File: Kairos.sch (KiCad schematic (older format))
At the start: 40 parts, among them J1 USB_mini_micro_B, Q1 NSS40301MZ4T1G, SW1 SW_RST1, U1 ATMEGA32U2-AU, Y1 Crystal

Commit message: Rotated ISO enter stabs
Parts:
- C1, C2, C3, C5, C6: footprint (none) -> Capacitors_SMD:C_0603
- C4: footprint (none) -> Capacitors_SMD:C_0805
- F1: footprint (none) -> Fuse_Holders_and_Fuses:Fuse_SMD1206_Reflow
- R1, R2, R3, R4: footprint (none) -> Resistors_SMD:R_0603
- U1: footprint (none) -> Housings_DFN_QFN:QFN-32-1EP_5x5mm_Pitch0.5mm
- Y1: footprint (none) -> Crystals:Crystal_SMD_5032-2pin_5.0x3.2mm
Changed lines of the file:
@@
 F 0 "U1" H 2200 4400 50  0000 C CNN
 F 1 "ATMEGA32U2-AU" H 3800 1700 50  0000 C CNN
-F 2 "" H 2900 3100 50  0001 C CNN
+F 2 "Housings_DFN_QFN:QFN-32-1EP_5x5mm_Pitch0.5mm" H 2900 3100 50  0001 C CNN
 F 3 "http://www.atmel.com/Images/doc7799.pdf" H 3150 1600 50  0001 C CNN
 	1    3050 3050
@@
 F 0 "R1" V 4480 3550 50  0000 C CNN
 F 1 "10k" V 4400 3550 50  0000 C CNN
-F 2 "" V 4330 3550 50  0001 C CNN
+F 2 "Resistors_SMD:R_0603" V 4330 3550 50  0001 C CNN
 F 3 "" H 4400 3550 50  0001 C CNN
 	1    4400 3550
@@
 F 0 "R2" V 1480 3450 50  0000 C CNN
 F 1 "22" V 1400 3450 50  0000 C CNN
-F 2 "" V 1330 3450 50  0001 C CNN
+F 2 "Resistors_SMD:R_0603" V 1330 3450 50  0001 C CNN
 F 3 "" H 1400 3450 50  0001 C CNN
 	1    1400 3450
@@
 F 0 "R3" V 1180 3550 50  0000 C CNN
 F 1 "22" V 1100 3550 50  0000 C CNN
-F 2 "" V 1030 3550 50  0001 C CNN
+F 2 "Resistors_SMD:R_0603" V 1030 3550 50  0001 C CNN
 F 3 "" H 1100 3550 50  0001 C CNN
 	1    1100 3550
@@
 F 0 "C1" V 1300 3300 50  0000 L CNN
 F 1 "1uF" V 1300 3050 50  0000 L CNN
-F 2 "" H 1388 3100 50  0001 C CNN
+F 2 "Capacitors_SMD:C_0603" H 1388 3100 50  0001 C CNN
 F 3 "" H 1350 3250 50  0001 C CNN
 	1    1350 3250
@@
 F 0 "R4" V 1480 2350 50  0000 C CNN
 F 1 "10k" V 1400 2350 50  0000 C CNN
-F 2 "" V 1330 2350 50  0001 C CNN
+F 2 "Resistors_SMD:R_0603" V 1330 2350 50  0001 C CNN
 F 3 "" H 1400 2350 50  0001 C CNN
 	1    1400 2350
@@
 F 0 "C2" H 725 1500 50  0000 L CNN
 F 1 "100nF" H 725 1300 50  0000 L CNN
-F 2 "" H 738 1250 50  0001 C CNN
+F 2 "Capacitors_SMD:C_0603" H 738 1250 50  0001 C CNN
 F 3 "" H 700 1400 50  0001 C CNN
 	1    700  1400
@@
 F 0 "C3" H 1025 1500 50  0000 L CNN
 F 1 "100nF" H 1025 1300 50  0000 L CNN
-F 2 "" H 1038 1250 50  0001 C CNN
+F 2 "Capacitors_SMD:C_0603" H 1038 1250 50  0001 C CNN
 F 3 "" H 1000 1400 50  0001 C CNN
 	1    1000 1400
@@
 F 0 "C4" H 1325 1500 50  0000 L CNN
 F 1 "4.7uF" H 1325 1300 50  0000 L CNN
-F 2 "" H 1338 1250 50  0001 C CNN
+F 2 "Capacitors_SMD:C_0805" H 1338 1250 50  0001 C CNN
 F 3 "" H 1300 1400 50  0001 C CNN
 	1    1300 1400
@@
 F 0 "Y1" H 1550 2850 50  0000 C CNN
 F 1 "Crystal" H 1550 2550 50  0000 C CNN
-F 2 "" H 1550 2700 50  0001 C CNN
+F 2 "Crystals:Crystal_SMD_5032-2pin_5.0x3.2mm" H 1550 2700 50  0001 C CNN
 F 3 "" H 1550 2700 50  0001 C CNN
 	1    1550 2700
@@
 F 0 "C6" H 1125 2650 50  0000 L CNN
 F 1 "22pF" H 1125 2450 50  0000 L CNN
-F 2 "" H 1138 2400 50  0001 C CNN
+F 2 "Capacitors_SMD:C_0603" H 1138 2400 50  0001 C CNN
 F 3 "" H 1100 2550 50  0001 C CNN
 	1    1100 2550
@@
 F 0 "C5" H 1125 2950 50  0000 L CNN
 F 1 "22pF" H 1125 2750 50  0000 L CNN
-F 2 "" H 1138 2700 50  0001 C CNN
+F 2 "Capacitors_SMD:C_0603" H 1138 2700 50  0001 C CNN
 F 3 "" H 1100 2850 50  0001 C CNN
 	1    1100 2850
@@
 F 0 "F1" V 1350 4300 50  0000 C CNN
 F 1 "Polyfuse" V 1550 4300 50  0000 C CNN
-F 2 "" H 1500 4100 50  0001 L CNN
+F 2 "Fuse_Holders_and_Fuses:Fuse_SMD1206_Reflow" H 1500 4100 50  0001 L CNN
 F 3 "" H 1450 4300 50  0001 C CNN
 	1    1450 4300

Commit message: Update associations for transistor and TQFP-ify the controller
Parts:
- Q1: footprint (none) -> TO_SOT_Packages_SMD:SOT-223-3Lead_TabPin2
- U1: footprint Housings_DFN_QFN:QFN-32-1EP_5x5mm_Pitch0.5mm -> Housings_QFP:TQFP-32_7x7mm_Pitch0.8mm
- Y1: footprint Crystals:Crystal_SMD_5032-2pin_5.0x3.2mm -> Crystals:Crystal_SMD_3225-4pin_3.2x2.5mm
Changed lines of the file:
@@
 F 0 "U1" H 2200 4400 50  0000 C CNN
 F 1 "ATMEGA32U2-AU" H 3800 1700 50  0000 C CNN
-F 2 "Housings_DFN_QFN:QFN-32-1EP_5x5mm_Pitch0.5mm" H 2900 3100 50  0001 C CNN
+F 2 "Housings_QFP:TQFP-32_7x7mm_Pitch0.8mm" H 2900 3100 50  0001 C CNN
 F 3 "http://www.atmel.com/Images/doc7799.pdf" H 3150 1600 50  0001 C CNN
 	1    3050 3050
@@
 F 0 "Y1" H 1550 2850 50  0000 C CNN
 F 1 "Crystal" H 1550 2550 50  0000 C CNN
-F 2 "Crystals:Crystal_SMD_5032-2pin_5.0x3.2mm" H 1550 2700 50  0001 C CNN
+F 2 "Crystals:Crystal_SMD_3225-4pin_3.2x2.5mm" H 1550 2700 50  0001 C CNN
 F 3 "" H 1550 2700 50  0001 C CNN
 	1    1550 2700
@@
 F 0 "Q1" H 4150 1275 50  0000 L CNN
 F 1 "NSS40301MZ4T1G" H 4150 1200 50  0000 L CNN
-F 2 "" H 4150 1125 50  0001 L CIN
+F 2 "TO_SOT_Packages_SMD:SOT-223-3Lead_TabPin2" H 4150 1125 50  0001 L CIN
 F 3 "" H 3950 1200 50  0001 L CNN
 	1    3950 1200

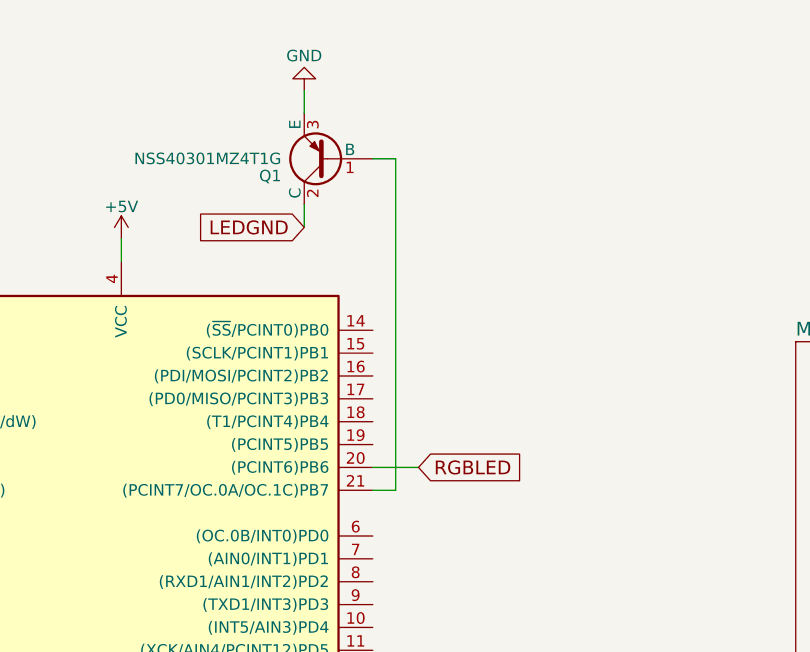
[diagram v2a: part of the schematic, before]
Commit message: Add missing 1.5k resistor on LED PWM
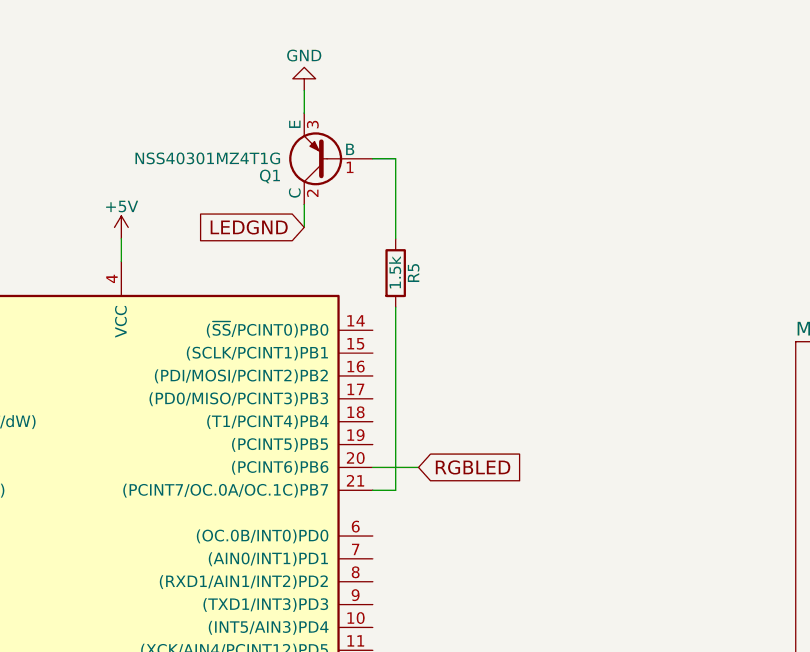
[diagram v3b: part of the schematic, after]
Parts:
- added R5: 1.5k, Resistors_SMD:R_0603, symbol R
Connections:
- net at U1.21 ((PCINT7/OC.0A/OC.1C)PB7): now also R5.2; no longer Q1.1 (B)
- new net: Q1.1 (B), R5.1
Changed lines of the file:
@@
 	4150 2650 4250 2650
-Wire Wire Line
-	4250 2650 4250 1200
 Wire Wire Line
 	4250 1200 4150 1200
@@
 NoConn ~ 1150 4600
 NoConn ~ 1150 4800
+$Comp
+L R R5
+U 1 1 59512333
+P 4250 1700
+F 0 "R5" V 4330 1700 50  0000 C CNN
+F 1 "1.5k" V 4250 1700 50  0000 C CNN
+F 2 "Resistors_SMD:R_0603" V 4180 1700 50  0001 C CNN
+F 3 "" H 4250 1700 50  0001 C CNN
+	1    4250 1700
+	1    0    0    -1
+$EndComp
+Wire Wire Line
+	4250 1200 4250 1550
+Wire Wire Line
+	4250 2650 4250 1850
 $EndSCHEMATC

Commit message: Fix the crystal
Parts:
- removed Y1: Crystal, Crystals:Crystal_SMD_3225-4pin_3.2x2.5mm, symbol Crystal
- added Y1: Crystal_GND24, Crystals:Crystal_SMD_3225-4pin_3.2x2.5mm, symbol Crystal_GND24
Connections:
- net GND: now also Y1.2, Y1.4
- net at C6.1, U1.1 (XTAL1): now also Y1.1
- net at C5.1, U1.2 (PC0(XTAL2)): now also Y1.3

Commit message: Add lib, update schematic
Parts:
- removed J1: USB_mini_micro_B, symbol USB_mini_micro_B
- added USB1: Molex-0548190589, symbol Molex-0548190589
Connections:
- net DM: now also USB1.4 (D-)
- net DP: now also USB1.3 (D+)
- net GND: now also USB1.1 (GND)
- net VCC: now also USB1.5 (VBUS)
- no-connect marks 3 -> 2
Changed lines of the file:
@@
 LIBS:ws2812b
 LIBS:keyboard_parts
+LIBS:Molex-0548190589
 LIBS:Kairos-cache
 EELAYER 25 0
@@
 $EndComp
 NoConn ~ 10000 6150
-$Comp
-L USB_mini_micro_B J1
-U 1 1 5947BA25
-P 1000 4450
-F 0 "J1" H 600 4400 60  0000 C CNN
-F 1 "USB_mini_micro_B" H 850 4700 60  0001 C CNN
-F 2 "" H 950 4450 60  0001 C CNN
-F 3 "" H 950 4450 60  0000 C CNN
-	1    1000 4450
-	1    0    0    -1
-$EndComp
 NoConn ~ 1150 4600
-NoConn ~ 1150 4800
 $Comp
 L R R5
@@
 	1350 2950 1350 2700
 Connection ~ 1950 2950
+$Comp
+L Molex-0548190589 USB1
+U 1 1 59859F20
+P 850 4500
+F 0 "USB1" H 850 4700 60  0000 C CNN
+F 1 "Molex-0548190589" H 850 4800 60  0000 C CNN
+F 2 "" H 850 4500 60  0001 C CNN
+F 3 "" H 850 4500 60  0001 C CNN
+	1    850  4500
+	0    -1   -1   0
+$EndComp
 $EndSCHEMATC

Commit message: Add that USB port
Not placed correctly yet
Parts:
- USB1: footprint (none) -> Molex-0548190589:Molex-0548190589
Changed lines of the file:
@@
 F 0 "USB1" H 850 4700 60  0000 C CNN
 F 1 "Molex-0548190589" H 850 4800 60  0000 C CNN
-F 2 "" H 850 4500 60  0001 C CNN
+F 2 "Molex-0548190589:Molex-0548190589" H 850 4500 60  0001 C CNN
 F 3 "" H 850 4500 60  0001 C CNN
 	1    850  4500

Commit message: Add reset button
Unlocked outline footprint to measure dimensions
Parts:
- SW1: footprint (none) -> Molex-0548190589:PushButton_6x6mm_TH
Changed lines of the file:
@@
 F 0 "SW1" H 1750 2260 50  0000 C CNN
 F 1 "SW_RST1" H 1600 2070 50  0000 C CNN
-F 2 "" H 1600 2150 60  0001 C CNN
+F 2 "Molex-0548190589:PushButton_6x6mm_TH" H 1600 2150 60  0001 C CNN
 F 3 "" H 1600 2150 60  0000 C CNN
 	1    1600 2150

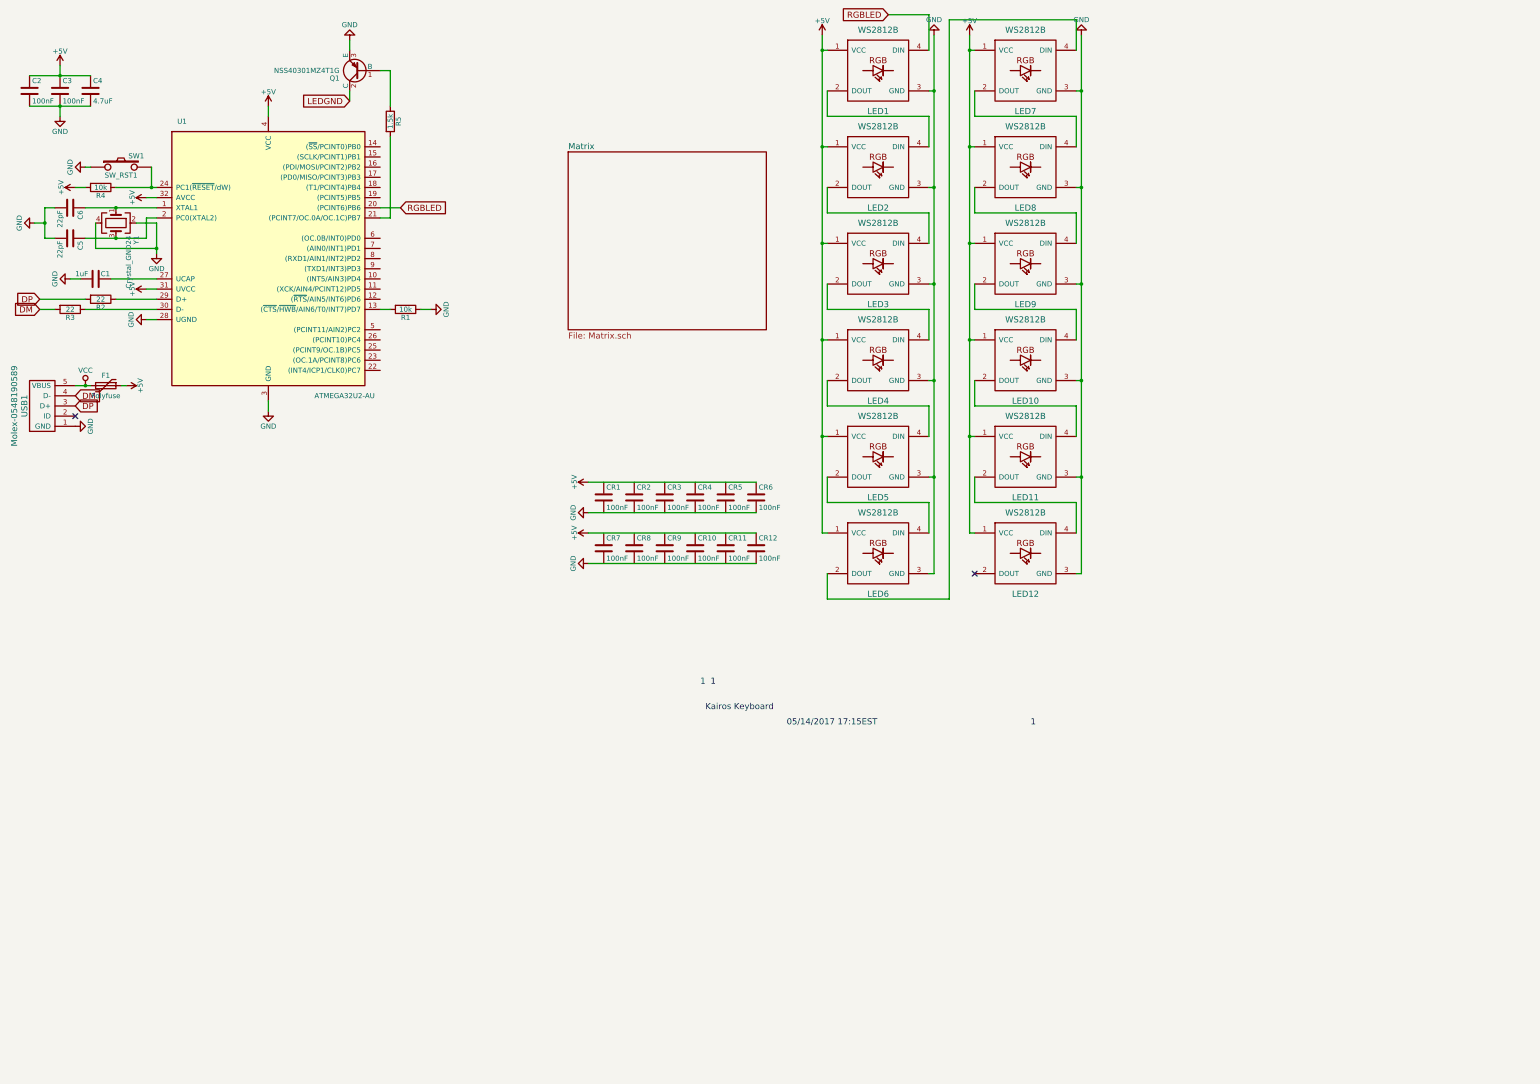
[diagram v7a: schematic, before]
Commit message: Add 2 more RGBs and their decoupling caps
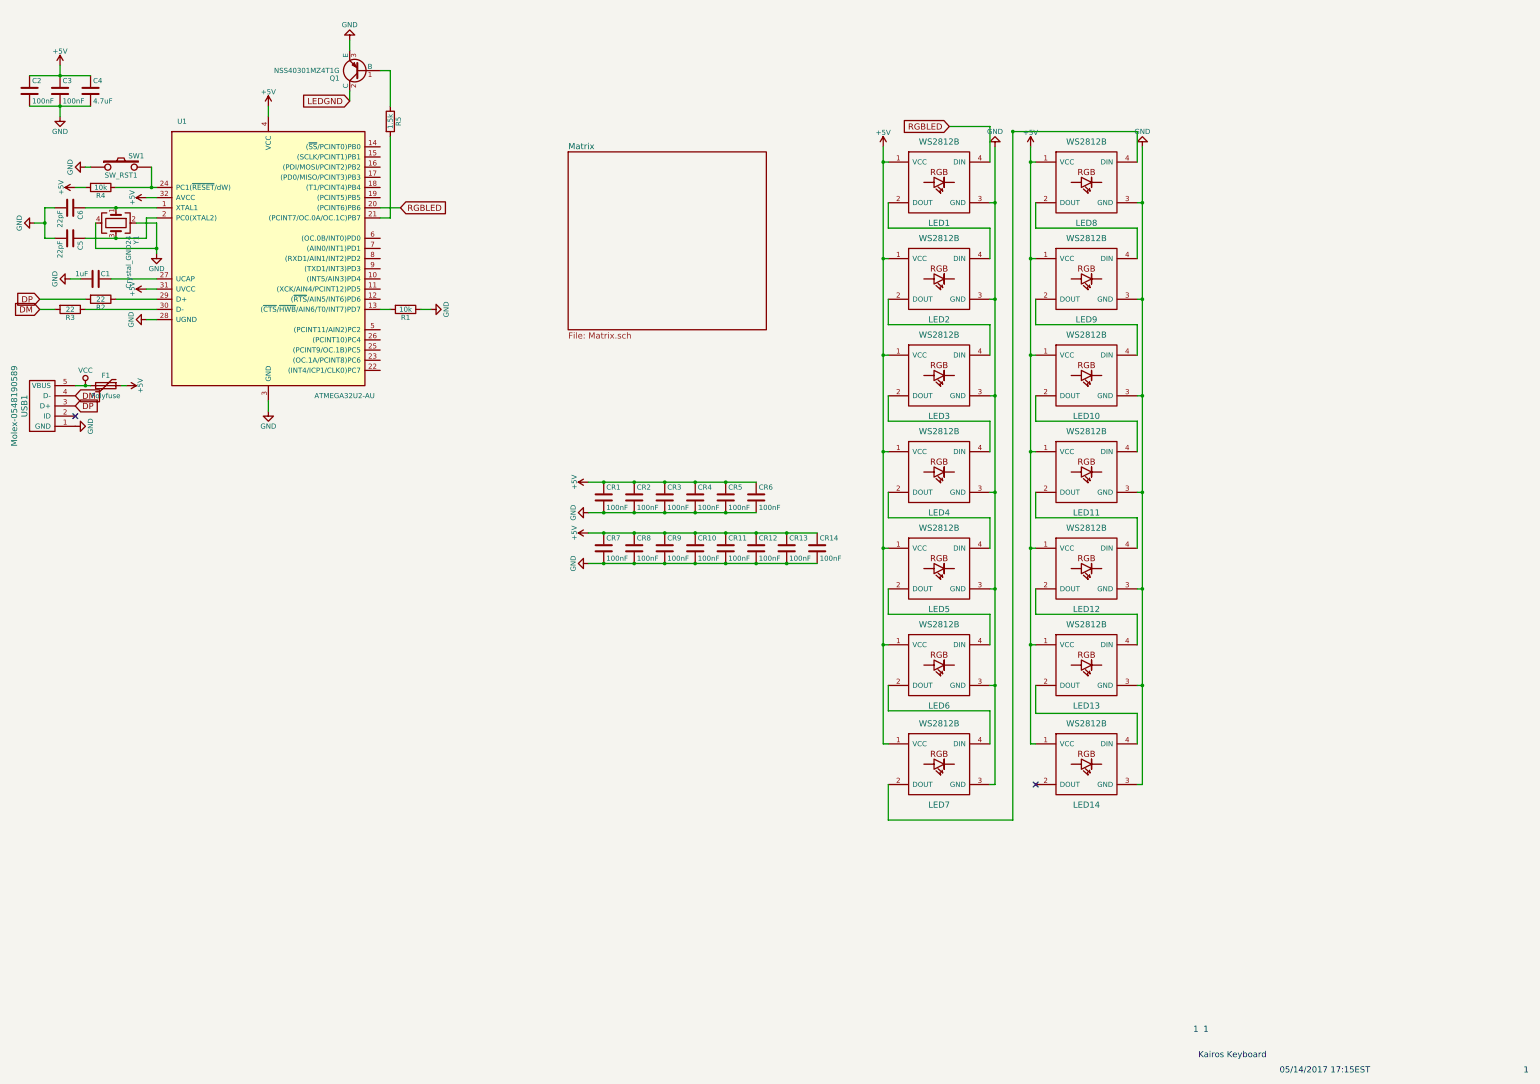
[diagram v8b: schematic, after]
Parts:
- added CR13, CR14: 100nF, symbol C
- added LED13, LED14: WS2812B, symbol WS2812B
- LED1, LED10, LED11, LED12, LED2, LED3, LED4, LED5, LED6, LED7, LED8, LED9: footprint (none) -> WS2812B:WS2812B
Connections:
- net +5V: now also CR1.1, CR10.1, CR11.1, CR2.1, CR3.1, CR4.1, CR5.1, CR7.1, CR8.1, CR9.1, CR13.1, CR14.1, LED13.1 (VCC), LED14.1 (VCC)
- net GND: now also CR1.2, CR10.2, CR11.2, CR2.2, CR3.2, CR4.2, CR5.2, CR7.2, CR8.2, CR9.2, CR13.2, CR14.2, LED13.3 (GND), LED14.3 (GND)
- net at LED12.2 (DOUT): now also LED13.4 (DIN)
- new net: LED13.2 (DOUT), LED14.4 (DIN)
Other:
- moved on the sheet: LED1, LED10, LED11, LED12, LED2, LED3, LED4, LED5, LED6, LED7, LED8, LED9
